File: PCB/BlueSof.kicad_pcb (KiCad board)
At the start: 2 copper layers, 134.3 x 100.2 mm, 117 parts, among them J1 USB_C_Receptacle_USB2.0, J2 Conn_01x01_Female, J3 Conn_01x04_Female, J4 Conn_01x01_Female, J5 USB_C_Receptacle_USB2.0, Q1 A03407, Q2 A03407, SW1 SW_PUSH, SW10 SW_PUSH, SW11 SW_PUSH, SW12 SW_PUSH, SW13 SW_PUSH, SW14 SW_PUSH, SW15 SW_PUSH, SW16 SW_PUSH, SW17 SW_PUSH, SW18 SW_PUSH, SW19 SW_PUSH, SW2 SW_PUSH, SW20 SW_PUSH, SW21 SW_PUSH, SW22 SW_PUSH, SW23 SW_PUSH, SW24 SW_PUSH, SW25 Rotary_Encoder_Switch, SW26 SW_PUSH, SW27 SW_PUSH, SW28 SW_PUSH, SW29 SW_PUSH, SW3 SW_PUSH, SW30 SW_PUSH, SW31 SW_Push, SW32 SW_Push, SW4 SW_PUSH, SW5 SW_PUSH, SW6 SW_PUSH, SW7 SW_PUSH, SW8 SW_PUSH, SW9 SW_PUSH, U1 LN2054Y42AMR, U2 E73-2G4M08S1C, U3 AP2112K-3.3, U4 E73-2G4M08S1C, U5 LN2054Y42AMR, U6 AP2112K-3.3, Y1 32.768kHz, Y2 32.768kHz

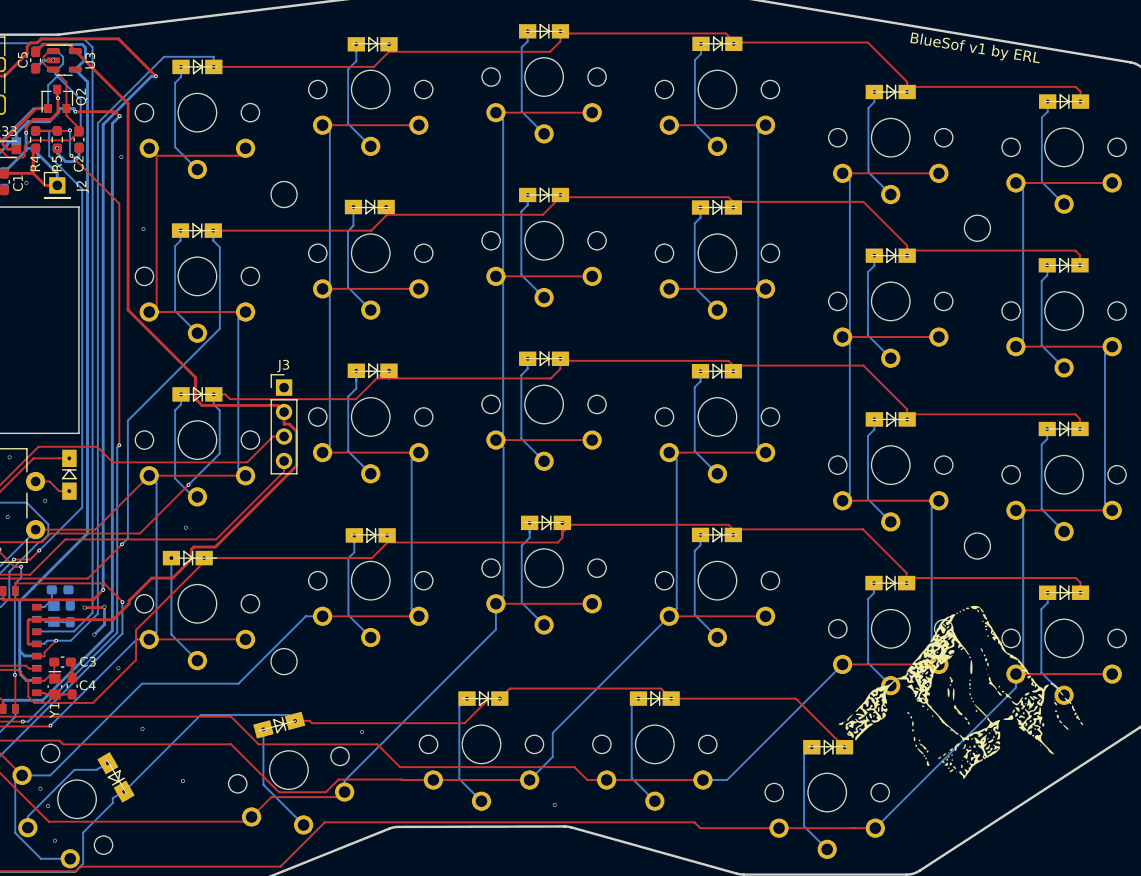
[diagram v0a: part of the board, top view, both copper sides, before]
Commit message: update to kicad6
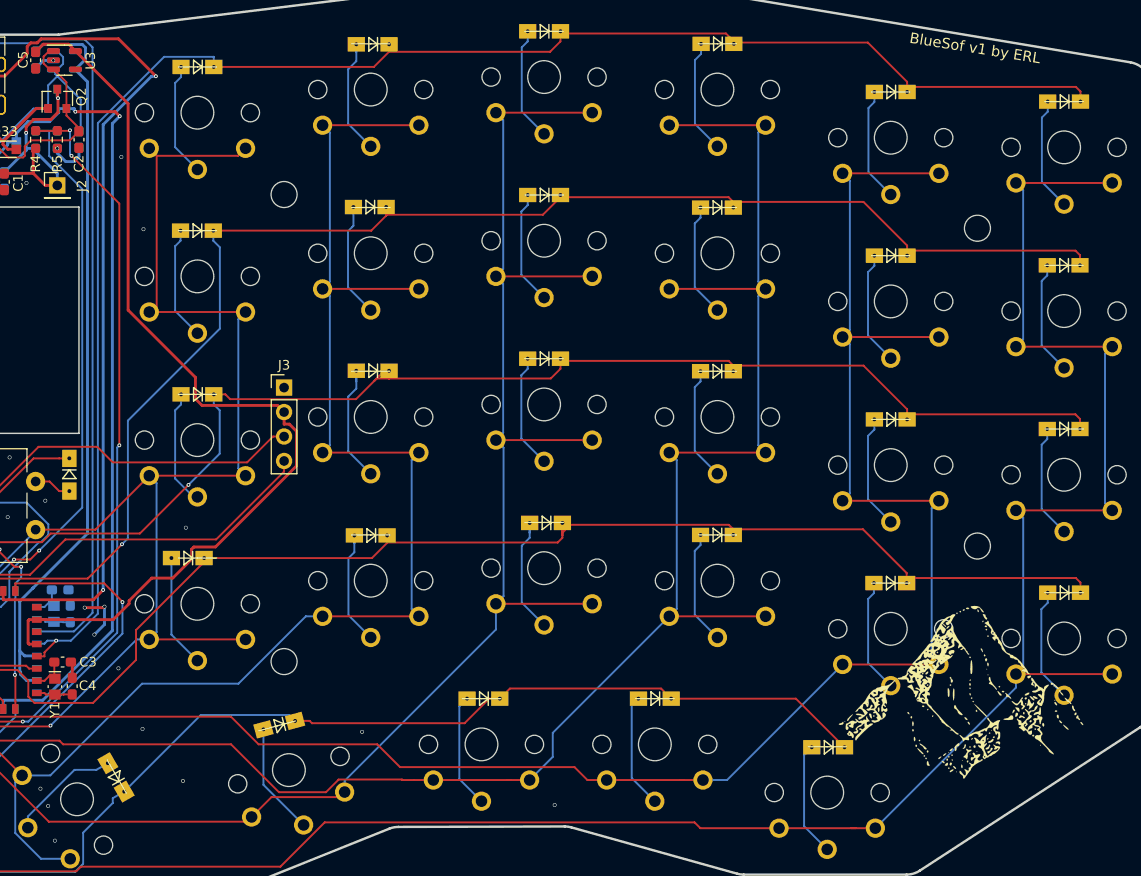
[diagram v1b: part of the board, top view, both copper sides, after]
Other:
- net class Default removed
- net class GND removed
- net class VCC removed

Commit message: first commit, side 1
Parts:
- removed ?: , 
- removed C10: 10uF, Capacitor_SMD:C_0603_1608Metric_Pad1.08x0.95mm_HandSolder
- removed C6, C7: 22pF, Capacitor_SMD:C_0603_1608Metric_Pad1.08x0.95mm_HandSolder
- removed C8, C9: 4.7uF, Capacitor_SMD:C_0603_1608Metric_Pad1.08x0.95mm_HandSolder
- removed D29, D30: D, BlueSof:Diode_SOD123
- removed D34, D36: LED, LED_SMD:LED_0603_1608Metric_Pad1.05x0.95mm_HandSolder
- removed D35: 1N5819, Diode_SMD:D_SOD-323_HandSoldering
- removed G*** (x2): LOGO, BlueSof:mountain
- removed J5: USB_C_Receptacle_USB2.0, Connector_USB:USB_C_Receptacle_HRO_TYPE-C-31-M-12
- removed Q1: A03407, Package_TO_SOT_SMD:SOT-23
- removed R10: 2M, Resistor_SMD:R_0603_1608Metric_Pad0.98x0.95mm_HandSolder
- removed R11, R15: 1k, Resistor_SMD:R_0603_1608Metric_Pad0.98x0.95mm_HandSolder
- removed R12, R13: 5.1k, Resistor_SMD:R_0603_1608Metric_Pad0.98x0.95mm_HandSolder
- removed R14: 100k, Resistor_SMD:R_0603_1608Metric_Pad0.98x0.95mm_HandSolder
- removed R16: 10k, Resistor_SMD:R_0603_1608Metric_Pad0.98x0.95mm_HandSolder
- removed R3: 820k, Resistor_SMD:R_0603_1608Metric_Pad0.98x0.95mm_HandSolder
- removed REF** (x5): MountingHole_2.7mm_M2.5, MountingHole:MountingHole_2.7mm_M2.5
- removed SW29, SW30: SW_PUSH, BlueSof:KailhLowProfile
- removed SW32: SW_Push, Button_Switch_SMD:SW_SPST_B3U-1000P
- removed U4: E73-2G4M08S1C, BlueSof:E73-2G4M08S1C-52840_NoInsidePads
- removed U5: LN2054Y42AMR, Package_TO_SOT_SMD:SOT-23-5
- removed U6: AP2112K-3.3, Package_TO_SOT_SMD:SOT-23-5
- removed Y2: 32.768kHz, Crystal:Crystal_SMD_MicroCrystal_CM9V-T1A-2Pin_1.6x1.0mm_HandSoldering
- added J9: Conn_01x04_Female, Connector_PinHeader_2.54mm:PinHeader_1x04_P2.54mm_Vertical, F.Cu at (4.53, 69.5)
- added SW59: SW_SPDT, Button_Switch_THT:SW_CuK_OS102011MA1QN1_SPDT_Angled, F.Cu at (54.2, 44.8)
- U2: footprint BlueSof:E73-2G4M08S1C-52840_NoInsidePads -> BlueSof:E73-2G4M08S1C-52840
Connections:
- J1 pad A8: (no net) -> no_connect_65
- J1 pad B8: (no net) -> no_connect_66
- Q2 pad 3: VBAT -> Net-(Q2-Pad3)
- U2 pad 10: ENCA -> row1
- U2 pad 25: (no net) -> DCCH
- U2 pad 33: row1 -> ENCA
- U2 pad 35: row2 -> ENCB
- U2 pad 9: ENCB -> row2
- U3 pad 4: (no net) -> no_connect_81
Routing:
- net col0: track 244.8 -> 0.00 mm, vias 1 -> 0
- net col1: track 211.1 -> 0.00 mm, vias 1 -> 0
- net col2: track 196.3 -> 0.00 mm, vias 1 -> 0
- net col3: track 181.0 -> 0.00 mm, vias 1 -> 0
- net row0: track 175.0 -> 0.00 mm, vias 1 -> 0
- net col4: track 167.2 -> 0.00 mm, vias 1 -> 0
- net row1: track 165.5 -> 0.00 mm, vias 2 -> 0
- net row4: track 157.8 -> 0.00 mm, vias 1 -> 0
- net row2: track 155.7 -> 0.00 mm, vias 4 -> 0
- net row3: track 152.5 -> 0.00 mm, vias 1 -> 0
- net col5: track 137.4 -> 0.00 mm, vias 1 -> 0
- net VBUS: track 129.8 -> 0.00 mm, vias 2 -> 0
- net VBUS2: track 118.0 -> 0.00 mm, vias 2 -> 0
- net DATA+: track 103.2 -> 0.00 mm, vias 5 -> 0
- net VDD_H: track 100.8 -> 0.00 mm
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
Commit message: EOD
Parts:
- added C10: 10uF, Capacitor_SMD:C_0603_1608Metric_Pad1.08x0.95mm_HandSolder, F.Cu at (-96.7, 59.6)
- added C6: 22pF, Capacitor_SMD:C_0603_1608Metric_Pad1.08x0.95mm_HandSolder, F.Cu at (-129.2, 92.2)
- added C7: 22pF, Capacitor_SMD:C_0603_1608Metric_Pad1.08x0.95mm_HandSolder, F.Cu at (-129.2, 89.7)
- added C8: 4.7uF, Capacitor_SMD:C_0603_1608Metric_Pad1.08x0.95mm_HandSolder, F.Cu at (-162.8, 124.2)
- added C9: 4.7uF, Capacitor_SMD:C_0603_1608Metric_Pad1.08x0.95mm_HandSolder, F.Cu at (-104.2, 67.2)
- added D29: D, BlueSof:Diode_SOD123, F.Cu at (-161.9, 121.6)
- added D30: D, BlueSof:Diode_SOD123, F.Cu at (-187.2, 134.7)
- added D34: D, BlueSof:Diode_SOD123, F.Cu at (-161.9, 119.1)
- added D35: D, BlueSof:Diode_SOD123, F.Cu at (-123.4, 77.4)
- added D36: D, BlueSof:Diode_SOD123, F.Cu at (-236.8, 130.9)
- added D37: D, BlueSof:Diode_SOD123, F.Cu at (-100.2, 54.5)
- added D38: D, BlueSof:Diode_SOD123, F.Cu at (-243.0, 136.0)
- added D39: D, BlueSof:Diode_SOD123, F.Cu at (-161.9, 116.5)
- added D40: D, BlueSof:Diode_SOD123, F.Cu at (-181.0, 134.7)
- added D41: D, BlueSof:Diode_SOD123, F.Cu at (-193.4, 134.7)
- added D42: LED, LED_SMD:LED_0603_1608Metric_Pad1.05x0.95mm_HandSolder, F.Cu at (-101.0, 57.1)
- added D43: D, BlueSof:Diode_SOD123, F.Cu at (-109.5, 64.7)
- added D44: D, BlueSof:Diode_SOD123, F.Cu at (-230.6, 130.9)
- added D45: D, BlueSof:Diode_SOD123, F.Cu at (-230.6, 136.0)
- added D46: D, BlueSof:Diode_SOD123, F.Cu at (-230.6, 133.4)
- added D47: D, BlueSof:Diode_SOD123, F.Cu at (-243.0, 130.9)
- added D48: D, BlueSof:Diode_SOD123, F.Cu at (-87.7, 44.1)
- added D49: D, BlueSof:Diode_SOD123, F.Cu at (-236.8, 136.0)
- added D50: D, BlueSof:Diode_SOD123, F.Cu at (-166.5, 128.8)
- added D51: D, BlueSof:Diode_SOD123, F.Cu at (-212.0, 134.7)
- added D52: D, BlueSof:Diode_SOD123, F.Cu at (-205.8, 134.7)
- added D53: 1N5819, Diode_SMD:D_SOD-323_HandSoldering, F.Cu at (-124.0, 80.2)
- added D54: LED, LED_SMD:LED_0603_1608Metric_Pad1.05x0.95mm_HandSolder, F.Cu at (-148.3, 108.9)
- added D55: D, BlueSof:Diode_SOD123, F.Cu at (-236.8, 133.4)
- added D56: D, BlueSof:Diode_SOD123, F.Cu at (-109.5, 62.2)
- added D57: D, BlueSof:Diode_SOD123, F.Cu at (-155.7, 116.5)
- added D58: D, BlueSof:Diode_SOD123, F.Cu at (-218.2, 134.7)
- added D59: D, BlueSof:Diode_SOD123, F.Cu at (-224.4, 134.7)
- added D60: D, BlueSof:Diode_SOD123, F.Cu at (-103.3, 62.2)
- added D61: D, BlueSof:Diode_SOD123, F.Cu at (-243.0, 133.4)
- added D62: D, BlueSof:Diode_SOD123, F.Cu at (-199.6, 134.7)
- added J10: Conn_01x01_Female, Connector_PinHeader_2.54mm:PinHeader_1x01_P2.54mm_Vertical, F.Cu at (-175.6, 135.7)
- added J5: Conn_01x04_Female, Connector_PinHeader_2.54mm:PinHeader_1x04_P2.54mm_Vertical, F.Cu at (-128.8, 78.5)
- added J6: Conn_01x04_Female, Connector_PinHeader_2.54mm:PinHeader_1x04_P2.54mm_Vertical, F.Cu at (-167.3, 117.6)
- added J7: USB_C_Receptacle_USB2.0, BlueSof:USB-C_C168688, F.Cu at (-144.7, 102.9)
- added J8: Conn_01x01_Female, Connector_PinHeader_2.54mm:PinHeader_1x01_P2.54mm_Vertical, F.Cu at (-124.2, 84.0)
- added Q1: A03407, Package_TO_SOT_SMD:SOT-23, F.Cu at (-94.8, 55.5)
- added R10: 2M, Resistor_SMD:R_0603_1608Metric_Pad0.98x0.95mm_HandSolder, F.Cu at (-110.4, 71.6)
- added R11: 1k, Resistor_SMD:R_0603_1608Metric_Pad0.98x0.95mm_HandSolder, F.Cu at (-136.6, 98.4)
- added R12: 5.1k, Resistor_SMD:R_0603_1608Metric_Pad0.98x0.95mm_HandSolder, F.Cu at (-82.4, 44.0)
- added R13: 5.1k, Resistor_SMD:R_0603_1608Metric_Pad0.98x0.95mm_HandSolder, F.Cu at (-101.1, 59.6)
- added R14: 100k, Resistor_SMD:R_0603_1608Metric_Pad0.98x0.95mm_HandSolder, F.Cu at (-148.3, 111.5)
- added R15: 1k, Resistor_SMD:R_0603_1608Metric_Pad0.98x0.95mm_HandSolder, F.Cu at (-110.4, 74.1)
- added R16: 10k, Resistor_SMD:R_0603_1608Metric_Pad0.98x0.95mm_HandSolder, F.Cu at (-167.4, 131.3)
- added R3: 820k, Resistor_SMD:R_0603_1608Metric_Pad0.98x0.95mm_HandSolder, F.Cu at (-104.2, 64.7)
- added SW29: Rotary_Encoder_Switch, Rotary_Encoder:RotaryEncoder_Alps_EC11E-Switch_Vertical_H20mm, F.Cu at (-129.1, 66.0)
- added SW30: SW_PUSH, BlueSof:KailhLowProfile, F.Cu at (-179.2, 88.1)
- added SW32: SW_PUSH, BlueSof:KailhLowProfile, F.Cu at (-179.2, 124.3)
- added SW33: SW_PUSH, BlueSof:KailhLowProfile, F.Cu at (-131.9, 51.9)
- added SW34: SW_PUSH, BlueSof:KailhLowProfile, F.Cu at (-208.4, 51.9)
- added SW35: SW_PUSH, BlueSof:KailhLowProfile, F.Cu at (-198.1, 70.0)
- added SW36: SW_PUSH, BlueSof:KailhLowProfile, F.Cu at (-170.2, 51.9)
- added SW37: SW_PUSH, BlueSof:KailhLowProfile, F.Cu at (-236.5, 84.3)
- added SW38: SW_PUSH, BlueSof:KailhLowProfile, F.Cu at (-217.4, 88.1)
- added SW39: SW_PUSH, BlueSof:KailhLowProfile_1.5U, F.Cu at (-232.0, 51.9)
- added SW40: SW_PUSH, BlueSof:KailhLowProfile, F.Cu at (-198.3, 124.3)
- added SW41: SW_PUSH, BlueSof:KailhLowProfile, F.Cu at (-236.5, 120.6)
- added SW42: SW_PUSH, BlueSof:KailhLowProfile, F.Cu at (-160.1, 106.2)
- added SW43: SW_PUSH, BlueSof:KailhLowProfile, F.Cu at (-159.8, 70.0)
- added SW44: SW_PUSH, BlueSof:KailhLowProfile, F.Cu at (-217.2, 70.0)
- added SW45: SW_Push, Button_Switch_SMD:SW_SPST_B3U-1000P, F.Cu at (-109.7, 68.2)
- added SW46: SW_PUSH, BlueSof:KailhLowProfile, F.Cu at (-140.9, 88.1)
- added SW47: SW_PUSH, BlueSof:KailhLowProfile, F.Cu at (-179.2, 106.2)
- added SW48: SW_PUSH, BlueSof:KailhLowProfile, F.Cu at (-160.1, 88.1)
- added SW49: SW_PUSH, BlueSof:KailhLowProfile, F.Cu at (-217.4, 106.2)
- added SW50: SW_PUSH, BlueSof:KailhLowProfile, F.Cu at (-151.1, 51.9)
- added SW51: SW_PUSH, BlueSof:KailhLowProfile, F.Cu at (-189.3, 51.9)
- added SW52: SW_PUSH, BlueSof:KailhLowProfile, F.Cu at (-198.3, 88.1)
- added SW53: SW_PUSH, BlueSof:KailhLowProfile, F.Cu at (-112.8, 51.9)
- added SW54: SW_PUSH, BlueSof:KailhLowProfile, F.Cu at (-178.9, 70.0)
- added SW55: SW_SPDT, Button_Switch_THT:SW_CuK_OS102011MA1QN1_SPDT_Angled, F.Cu at (-99.0, 46.0)
- added SW56: SW_PUSH, BlueSof:KailhLowProfile, F.Cu at (-198.3, 106.2)
- added SW57: SW_PUSH, BlueSof:KailhLowProfile, F.Cu at (-236.5, 102.4)
- added SW58: SW_PUSH, BlueSof:KailhLowProfile, F.Cu at (-217.4, 124.3)
- added SW60: SW_PUSH, BlueSof:KailhLowProfile, F.Cu at (-140.7, 70.0)
- added U4: E73-2G4M08S1C, BlueSof:E73-2G4M08S1C-52840, F.Cu at (-245.3, 68.1)
- added U5: LN2054Y42AMR, Package_TO_SOT_SMD:SOT-23-5, F.Cu at (-117.7, 78.4)
- added U6: AP2112K-3.3, Package_TO_SOT_SMD:SOT-23-5, F.Cu at (-88.2, 47.6)
- added Y2: 32.768kHz, Crystal:Crystal_SMD_MicroCrystal_CM9V-T1A-2Pin_1.6x1.0mm_HandSoldering, F.Cu at (-119.7, 83.1)
- J1: footprint Connector_USB:USB_C_Receptacle_HRO_TYPE-C-31-M-12 -> BlueSof:USB-C_C168688
- moved J9 128.7 mm to (130.5, 95.7)
- moved SW59 79.7 mm to (89.4, 116.3), turned to -90 degrees
- moved D31 66.8 mm to (95.3, 116.2)
- moved R1 63.7 mm to (98.8, 116.2)
- moved D32 61.5 mm to (95.3, 111.2)
- moved R6 58.4 mm to (98.8, 111.2)
- moved C3 45.7 mm to (106.6, 65.5)
- moved C4 45.7 mm to (107.6, 68.0)
- moved U2 45.7 mm to (104.3, 64.2)
- moved Y1 45.7 mm to (105.8, 68.0)
- moved J4 41.3 mm to (110.1, 98.2), turned to 0 degrees
- moved J2 33.1 mm to (110.1, 94.6), turned to -90 degrees
- moved R2 15.2 mm to (110.1, 61.2), turned to 180 degrees
- moved D25 12.6 mm to (110.1, 104.2)
- moved U1 12.1 mm to (110.0, 58.6), turned to 0 degrees
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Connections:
- net no_connect_65 renamed no_connect_104
- net no_connect_66 renamed no_connect_105
- net no_connect_67 renamed no_connect_108
- net no_connect_68 renamed no_connect_109
- net no_connect_69 renamed no_connect_110
- net no_connect_70 renamed no_connect_111
- net no_connect_71 renamed no_connect_112
- net no_connect_72 renamed no_connect_113
- net no_connect_73 renamed no_connect_114
- net no_connect_74 renamed no_connect_115
- net no_connect_75 renamed no_connect_116
- net no_connect_76 renamed no_connect_117
- net no_connect_77 renamed no_connect_118
- net no_connect_78 renamed no_connect_119
- net no_connect_79 renamed no_connect_120
- net no_connect_80 renamed no_connect_121
- net no_connect_81 renamed no_connect_122
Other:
- outline, holes or cut-outs redrawn
- board text added: "BlueSof v2 by ERL"

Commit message: getting close to layout on side 1
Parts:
- added REF**: mouseBit_2.5mm, BlueSof:mouseBit_2.5mm, F.Cu at (86.2, 104.8)
- added REF**: mouseBit_2.5mm, BlueSof:mouseBit_2.5mm, F.Cu at (86.2, 87.8)
- added REF**: mouseBit_2.5mm, BlueSof:mouseBit_2.5mm, F.Cu at (86.2, 70.8)
- added REF**: breakaway-mousebites, Keebio-Parts:breakaway-mousebites, F.Cu at (92.0, 71.8)
- added REF**: mouseBit_2.5mm, BlueSof:mouseBit_2.5mm, F.Cu at (86.2, 53.8)
- added REF**: mouseBit_2.5mm, BlueSof:mouseBit_2.5mm, F.Cu at (86.2, 121.6)
- D1, D10, D11, D12, D13, D14, D15, D16, D17, D18, D19, D2, D20, D21, D22, D23, D24, D25, D26, D27, D28, D29, D3, D30, D34, D35, D36, D37, D38, D39, D4, D40, D41, D43, D44, D45, D46, D47, D48, D49, D5, D50, D51, D52, D55, D56, D57, D58, D59, D6, D60, D61, D62, D7, D8, D9: footprint BlueSof:Diode_SOD123 -> Diode_SMD:D_SOD-123
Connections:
- C10 pad 1: VDD_H -> VDD_H_LEFT
- C10 pad 2: GND -> GND2
- C6 pad 1: GND -> GND2
- C7 pad 1: GND -> GND2
- C8 pad 1: VBAT -> VBAT_LEFT
- C8 pad 2: GND -> GND2
- C9 pad 2: GND -> GND2
- D1 pad 2: Net-(D1-Pad2) -> col4
- D16 pad 2: Net-(D16-Pad2) -> Net-(SW17-Pad1)
- D17 pad 2: Net-(D17-Pad2) -> Net-(SW18-Pad1)
- D19 pad 2: Net-(D19-Pad2) -> Net-(SW20-Pad1)
- D2 pad 2: Net-(D2-Pad2) -> col3
- D20 pad 2: Net-(D20-Pad2) -> Net-(SW20-Pad2)
- D21 pad 2: Net-(D21-Pad2) -> Net-(SW22-Pad1)
- D22 pad 2: Net-(D22-Pad2) -> col1
- D23 pad 2: Net-(D23-Pad2) -> col0
- D26 pad 2: Net-(D26-Pad2) -> col3
- D27 pad 2: Net-(D27-Pad2) -> col2
- D29 pad 1: row0 -> row0_LEFT
- D29 pad 2: Net-(D29-Pad2) -> col4_LEFT
- D3 pad 2: Net-(D3-Pad2) -> col2
- D30 pad 1: row1 -> row1_LEFT
- D30 pad 2: Net-(D30-Pad2) -> Net-(SW36-Pad1)
- D34 pad 1: row2 -> row2_LEFT
- D34 pad 2: Net-(D34-Pad2) -> Net-(SW37-Pad1)
- D35 pad 1: row3 -> row3_LEFT
- D35 pad 2: Net-(D35-Pad2) -> Net-(SW38-Pad1)
- D36 pad 1: row4 -> row4_LEFT
- D37 pad 1: row0 -> row0_LEFT
- D37 pad 2: Net-(D37-Pad2) -> col3_LEFT
- D38 pad 1: row1 -> row1_LEFT
- D38 pad 2: Net-(D38-Pad2) -> Net-(SW36-Pad2)
- D39 pad 1: row2 -> row2_LEFT
- D39 pad 2: Net-(D39-Pad2) -> Net-(SW37-Pad2)
- D4 pad 2: Net-(D4-Pad2) -> col1
- D40 pad 1: row3 -> row3_LEFT
- D41 pad 1: row4 -> row4_LEFT
- D41 pad 2: Net-(D41-Pad2) -> col3_LEFT
- D42 pad 2: P0.05 -> P0.05_LEFT
- D43 pad 1: row0 -> row0_LEFT
- D43 pad 2: Net-(D43-Pad2) -> col2_LEFT
- D44 pad 1: row1 -> row1_LEFT
- D45 pad 1: row2 -> row2_LEFT
- D46 pad 1: row3 -> row3_LEFT
- D47 pad 1: row4 -> row4_LEFT
- D47 pad 2: Net-(D47-Pad2) -> col2_LEFT
- D48 pad 1: row0 -> row0_LEFT
- D48 pad 2: Net-(D48-Pad2) -> col1_LEFT
- D49 pad 1: row1 -> row1_LEFT
- D5 pad 2: Net-(D5-Pad2) -> col0
- D50 pad 1: row2 -> row2_LEFT
- D51 pad 1: row3 -> row3_LEFT
- D51 pad 2: Net-(D51-Pad2) -> col1_LEFT
- D52 pad 1: row4 -> row4_LEFT
- D53 pad 2: VBUS -> VBUS_LEFT
- D54 pad 2: VBUS -> VBUS_LEFT
- D55 pad 1: row0 -> row0_LEFT
- D55 pad 2: Net-(D55-Pad2) -> col0_LEFT
- D56 pad 1: row1 -> row1_LEFT
- D56 pad 2: Net-(D56-Pad2) -> Net-(SW57-Pad1)
- D57 pad 1: row2 -> row2_LEFT
- D58 pad 1: row3 -> row3_LEFT
- D58 pad 2: Net-(D58-Pad2) -> col0_LEFT
- D59 pad 1: row0 -> row0_LEFT
- D60 pad 1: row1 -> row1_LEFT
- D61 pad 1: row2 -> row2_LEFT
- D62 pad 1: row3 -> row3_LEFT
- D8 pad 2: Net-(D8-Pad2) -> Net-(SW8-Pad2)
- J1 pad A8: no_connect_104 -> no_connect_113
- J1 pad B8: no_connect_105 -> no_connect_114
- J10 pad 1: GND -> GND2
- J5 pad 1: GND -> GND2
- J5 pad 2: VBUS -> VBUS_LEFT
- J5 pad 3: DATA+ -> DATA+_LEFT
- J5 pad 4: DATA- -> DATA-_LEFT
- J6 pad 1: GND -> GND2
- J6 pad 2: VDD_H -> VDD_H_LEFT
- J6 pad 3: SWD -> SWD_LEFT
- J6 pad 4: SWC -> SWC_LEFT
- J7 pad A1: GND -> GND2
- J7 pad A4: VBUS -> VBUS_LEFT
- J7 pad A6: DATA+ -> DATA+_LEFT
- J7 pad A7: DATA- -> DATA-_LEFT
- J7 pad A8: no_connect_106 -> no_connect_115
- J7 pad B6: DATA+ -> DATA+_LEFT
- J7 pad B7: DATA- -> DATA-_LEFT
- J7 pad B8: no_connect_107 -> no_connect_116
- J7 pad S1: GND -> GND2
- J8 pad 1: VBAT -> VBAT_LEFT
- Q1 pad 1: VBUS -> VBUS_LEFT
- R10 pad 1: BATTERY_MEASURE -> BATTERY_MEASURE_LEFT
- R10 pad 2: GND -> GND2
- R11 pad 2: GND -> GND2
- R14 pad 1: VBUS -> VBUS_LEFT
- R14 pad 2: GND -> GND2
- R16 pad 2: GND -> GND2
- R3 pad 1: VBAT -> VBAT_LEFT
- R3 pad 2: BATTERY_MEASURE -> BATTERY_MEASURE_LEFT
- SW1 pad 2: Net-(D1-Pad2) -> col4
- SW10 pad 1: col2 -> Net-(D9-Pad2)
- SW11 pad 1: col1 -> Net-(D10-Pad2)
- SW12 pad 1: col0 -> Net-(D11-Pad2)
- SW14 pad 1: col4 -> Net-(D13-Pad2)
- SW15 pad 1: col3 -> Net-(D14-Pad2)
- SW16 pad 1: col2 -> Net-(D15-Pad2)
- SW16 pad 2: Net-(D16-Pad2) -> Net-(SW17-Pad1)
- SW17 pad 1: col1 -> Net-(SW17-Pad1)
- SW17 pad 2: Net-(D17-Pad2) -> Net-(SW18-Pad1)
- SW18 pad 1: col0 -> Net-(SW18-Pad1)
- SW19 pad 2: Net-(D19-Pad2) -> Net-(SW20-Pad1)
- SW2 pad 2: Net-(D2-Pad2) -> col3
- SW20 pad 1: col4 -> Net-(SW20-Pad1)
- SW20 pad 2: Net-(D20-Pad2) -> Net-(SW20-Pad2)
- SW21 pad 1: col3 -> Net-(SW20-Pad2)
- SW21 pad 2: Net-(D21-Pad2) -> Net-(SW22-Pad1)
- SW22 pad 1: col2 -> Net-(SW22-Pad1)
- SW22 pad 2: Net-(D22-Pad2) -> col1
- SW23 pad 2: Net-(D23-Pad2) -> col0
- SW26 pad 2: Net-(D26-Pad2) -> col3
- SW27 pad 2: Net-(D27-Pad2) -> col2
- SW28 pad 2: Net-(D28-Pad2) -> Net-(SW28-Pad2)
- SW29 pad A: ENCA -> ENCA_LEFT
- SW29 pad B: ENCB -> ENCB_LEFT
- SW29 pad C: GND -> GND2
- SW29 pad S1: col5 -> col5_LEFT
- SW3 pad 2: Net-(D3-Pad2) -> col2
- SW30 pad 1: col5 -> col5_LEFT
- SW30 pad 2: Net-(D29-Pad2) -> col4_LEFT
- SW32 pad 1: col5 -> col5_LEFT
- SW32 pad 2: Net-(D30-Pad2) -> Net-(SW36-Pad1)
- SW33 pad 1: col5 -> col5_LEFT
- SW33 pad 2: Net-(D34-Pad2) -> Net-(SW37-Pad1)
- SW34 pad 1: col5 -> col5_LEFT
- SW34 pad 2: Net-(D35-Pad2) -> Net-(SW38-Pad1)
- SW35 pad 1: col4 -> col4_LEFT
- SW35 pad 2: Net-(D37-Pad2) -> col3_LEFT
- SW36 pad 1: col4 -> Net-(SW36-Pad1)
- SW36 pad 2: Net-(D38-Pad2) -> Net-(SW36-Pad2)
- SW37 pad 1: col4 -> Net-(SW37-Pad1)
- SW37 pad 2: Net-(D39-Pad2) -> Net-(SW37-Pad2)
- SW38 pad 1: col4 -> Net-(SW38-Pad1)
- SW39 pad 1: col4 -> col4_LEFT
- SW39 pad 2: Net-(D41-Pad2) -> col3_LEFT
- SW4 pad 2: Net-(D4-Pad2) -> col1
- SW40 pad 1: col3 -> col3_LEFT
- SW40 pad 2: Net-(D43-Pad2) -> col2_LEFT
- SW41 pad 1: col3 -> Net-(SW36-Pad2)
- SW42 pad 1: col3 -> Net-(SW37-Pad2)
- SW43 pad 1: col3 -> Net-(D40-Pad2)
- SW44 pad 1: col3 -> col3_LEFT
- SW44 pad 2: Net-(D47-Pad2) -> col2_LEFT
- SW45 pad 1: RESET -> RESET_LEFT
- SW45 pad 2: GND -> GND2
- SW46 pad 1: col2 -> col2_LEFT
- SW46 pad 2: Net-(D48-Pad2) -> col1_LEFT
- SW47 pad 1: col2 -> Net-(D44-Pad2)
- SW47 pad 2: Net-(D49-Pad2) -> Net-(SW47-Pad2)
- SW48 pad 1: col2 -> Net-(D45-Pad2)
- SW49 pad 1: col2 -> Net-(D46-Pad2)
- SW49 pad 2: Net-(D51-Pad2) -> col1_LEFT
- SW5 pad 2: Net-(D5-Pad2) -> col0
- SW50 pad 1: col2 -> col2_LEFT
- SW51 pad 1: col1 -> col1_LEFT
- SW51 pad 2: Net-(D55-Pad2) -> col0_LEFT
- SW52 pad 1: col1 -> Net-(D49-Pad2)
- SW52 pad 2: Net-(D56-Pad2) -> Net-(SW57-Pad1)
- SW53 pad 1: col1 -> Net-(D50-Pad2)
- SW54 pad 1: col1 -> col1_LEFT
- SW54 pad 2: Net-(D58-Pad2) -> col0_LEFT
- SW55 pad 1: VBAT -> VBAT_LEFT
- SW56 pad 1: col0 -> col0_LEFT
- SW57 pad 1: col0 -> Net-(SW57-Pad1)
- SW58 pad 1: col0 -> Net-(D57-Pad2)
- SW60 pad 1: col0 -> col0_LEFT
- SW8 pad 1: col4 -> Net-(D7-Pad2)
- SW8 pad 2: Net-(D8-Pad2) -> Net-(SW8-Pad2)
- SW9 pad 1: col3 -> Net-(SW8-Pad2)
- U2 pad 12: no_connect_108 -> no_connect_117
- U2 pad 14: no_connect_109 -> no_connect_118
- U2 pad 16: no_connect_110 -> no_connect_119
- U2 pad 18: no_connect_111 -> no_connect_120
- U2 pad 20: no_connect_112 -> no_connect_121
- U2 pad 22: no_connect_113 -> no_connect_122
- U2 pad 28: no_connect_114 -> no_connect_123
- U2 pad 30: no_connect_115 -> no_connect_124
- U2 pad 32: no_connect_116 -> no_connect_125
- U2 pad 34: no_connect_117 -> no_connect_126
- U2 pad 36: no_connect_118 -> no_connect_127
- U2 pad 38: no_connect_119 -> no_connect_128
- U2 pad 40: no_connect_120 -> no_connect_129
- U2 pad 42: no_connect_121 -> no_connect_130
- U3 pad 4: no_connect_122 -> no_connect_131
- U4 pad 1: col0 -> col0_LEFT
- U4 pad 10: row1 -> row1_LEFT
- U4 pad 12: no_connect_123 -> no_connect_132
- U4 pad 14: no_connect_124 -> no_connect_133
- U4 pad 15: P0.05 -> P0.05_LEFT
- U4 pad 16: no_connect_125 -> no_connect_134
- U4 pad 17: row0 -> row0_LEFT
- U4 pad 18: no_connect_126 -> no_connect_135
- U4 pad 19: VDD_H -> VDD_H_LEFT
- U4 pad 2: col1 -> col1_LEFT
- U4 pad 20: no_connect_127 -> no_connect_136
- U4 pad 21: GND -> GND2
- U4 pad 22: no_connect_128 -> no_connect_137
- U4 pad 23: VDD_H -> VDD_H_LEFT
- U4 pad 24: GND -> GND2
- U4 pad 25: DCCH -> DCCH_LEFT
- U4 pad 26: RESET -> RESET_LEFT
- U4 pad 27: VBUS -> VBUS_LEFT
- U4 pad 28: no_connect_129 -> no_connect_138
- U4 pad 29: DATA- -> DATA-_LEFT
- U4 pad 3: col2 -> col2_LEFT
- U4 pad 30: no_connect_130 -> no_connect_139
- U4 pad 31: DATA+ -> DATA+_LEFT
- U4 pad 32: no_connect_131 -> no_connect_140
- U4 pad 33: ENCA -> ENCA_LEFT
- U4 pad 34: no_connect_132 -> no_connect_141
- U4 pad 35: ENCB -> ENCB_LEFT
- U4 pad 36: no_connect_133 -> no_connect_142
- U4 pad 37: SWD -> SWD_LEFT
- U4 pad 38: no_connect_134 -> no_connect_143
- U4 pad 39: SWC -> SWC_LEFT
- U4 pad 4: col3 -> col3_LEFT
- U4 pad 40: no_connect_135 -> no_connect_144
- U4 pad 41: row3 -> row3_LEFT
- U4 pad 42: no_connect_136 -> no_connect_145
- U4 pad 43: row4 -> row4_LEFT
- U4 pad 5: GND -> GND2
- U4 pad 6: col4 -> col4_LEFT
- U4 pad 7: col5 -> col5_LEFT
- U4 pad 8: BATTERY_MEASURE -> BATTERY_MEASURE_LEFT
- U4 pad 9: row2 -> row2_LEFT
- U5 pad 2: GND -> GND2
- U5 pad 3: VBAT -> VBAT_LEFT
- U5 pad 4: VBUS -> VBUS_LEFT
- U6 pad 2: GND -> GND2
- U6 pad 4: no_connect_137 -> no_connect_146
- U6 pad 5: VDD_H -> VDD_H_LEFT
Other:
- outline, holes or cut-outs redrawn
